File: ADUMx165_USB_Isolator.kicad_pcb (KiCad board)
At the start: 4 copper layers, 50 x 36.5 mm, 62 parts, among them J1 XKB_U262-16XN-4BVC11, J2 HRO_TYPE-C-31-M-17, J3 XKB_U221-041N-4V33, J4 XKB_U221-041N-4V33, J5 XKB_U221-041N-4V33, J6 XKB_U221-041N-4V33, T1 DA2303-AL, U1 SN6505BDBV, U10 USBLC6-2P6, U2 USBLC6-2P6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

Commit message: Update readme.md Add Eng translation Add board image Change R7 value to 2K
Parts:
- R7: value 220R -> 2K

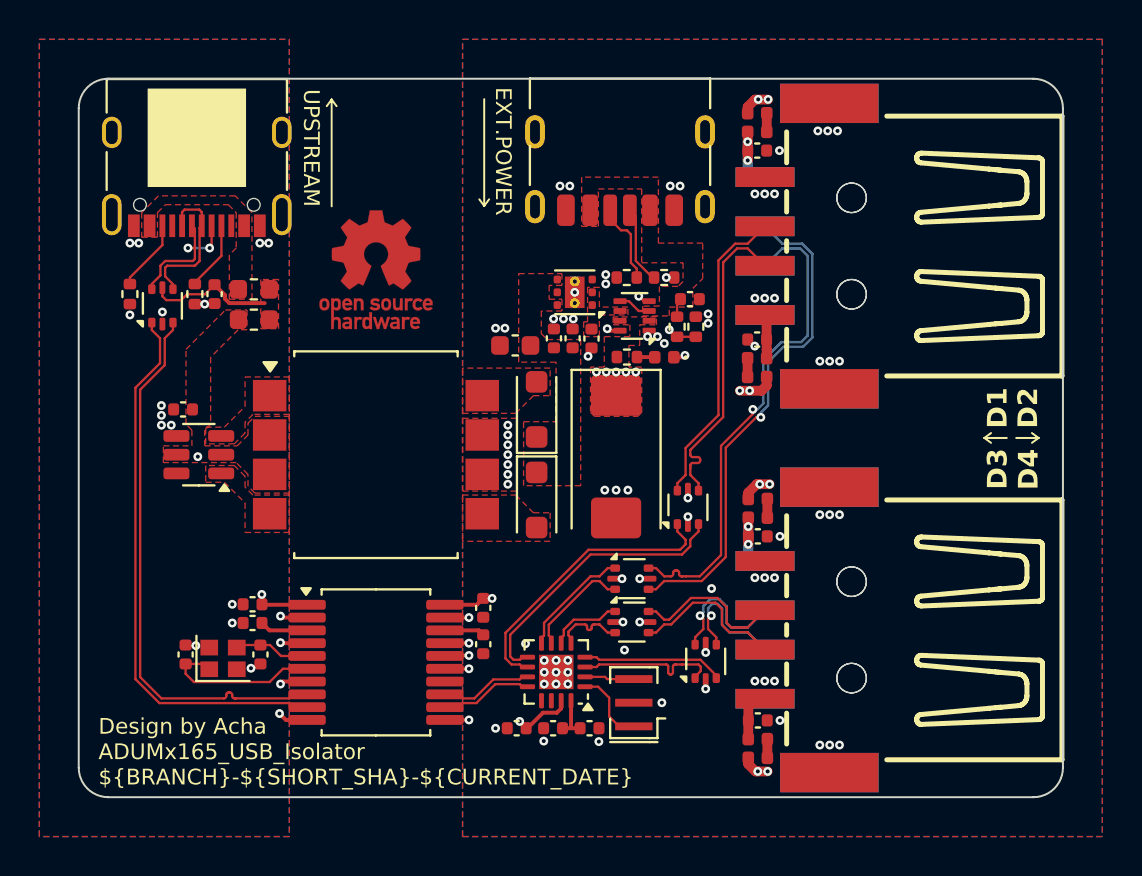
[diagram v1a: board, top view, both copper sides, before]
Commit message: Change TLV76750 to TLV76701
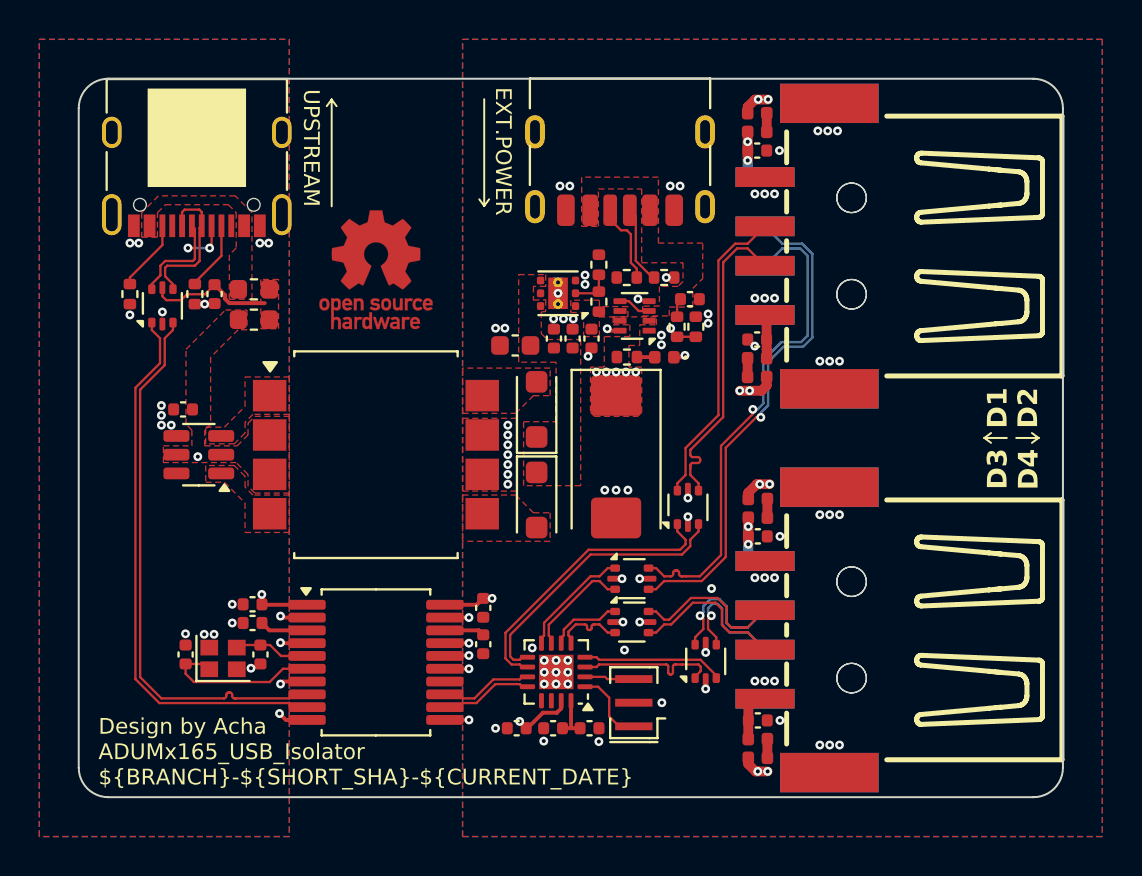
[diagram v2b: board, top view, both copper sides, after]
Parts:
- added R8: 110K, Resistor_SMD:R_0402_1005Metric, F.Cu at (136.4, 110.8)
- added R9: 20K, Resistor_SMD:R_0402_1005Metric, F.Cu at (136.4, 109.0)
- moved U4 0.85 mm to (134.3, 110.4)
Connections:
- U4 pad 2: +5V -> Net-(U4-FB)
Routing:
- net Net-(U4-FB): track 0.00 -> 2.09 mm
- net GND2: vias 82 -> 81
- net GND1: vias 19 -> 21
